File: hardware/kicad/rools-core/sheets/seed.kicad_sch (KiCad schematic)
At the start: 1 part

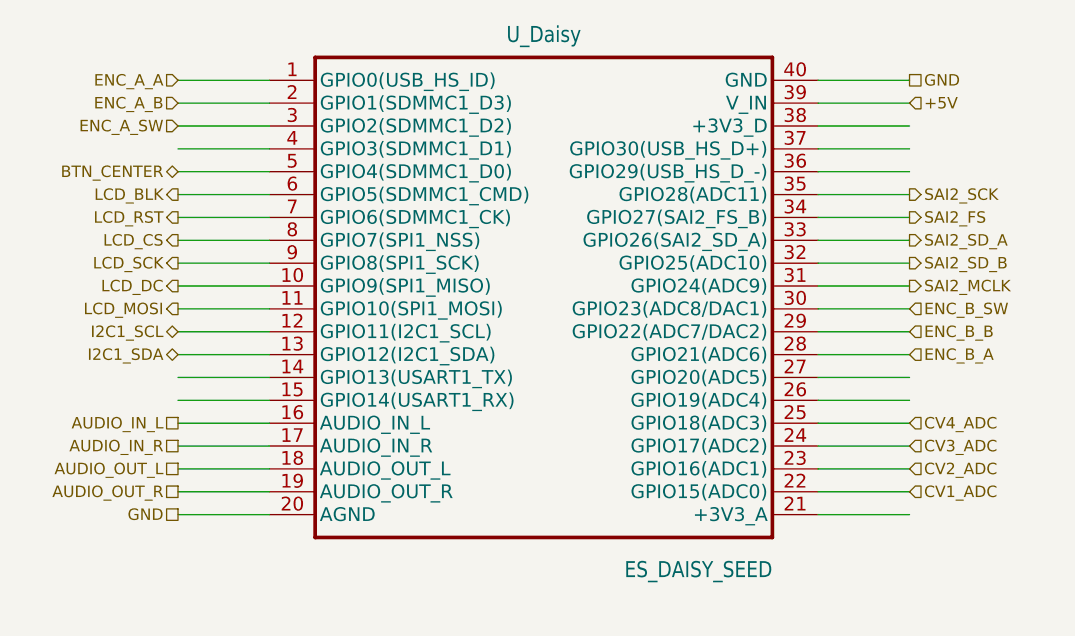
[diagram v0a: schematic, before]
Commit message: Wire rools-core KiCad sheets with global labels and UI peripherals.
Migrate inter-sheet nets to global labels and flesh out UI, power, and
child-sheet power entry so net names align with pins.h for PCB routing.

Co-authored-by: Cursor <cursoragent@cursor.com>
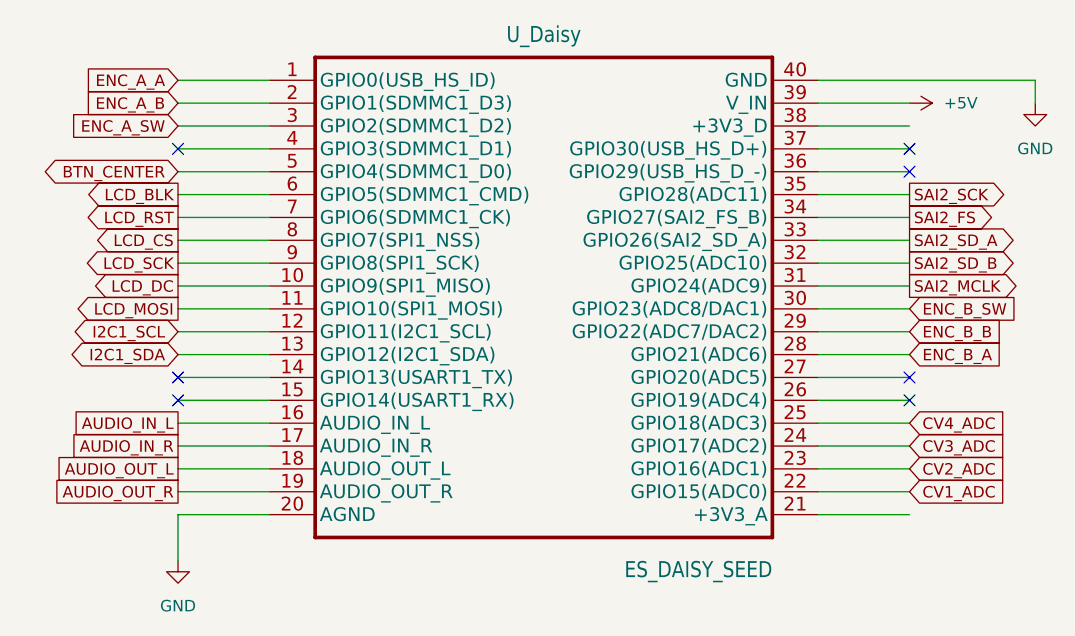
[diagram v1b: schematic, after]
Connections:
- no-connect marks 0 -> 7

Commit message: Add QSPI settings persistence, CV calibration app, and CV output driver.
Co-authored-by: Cursor <cursoragent@cursor.com>
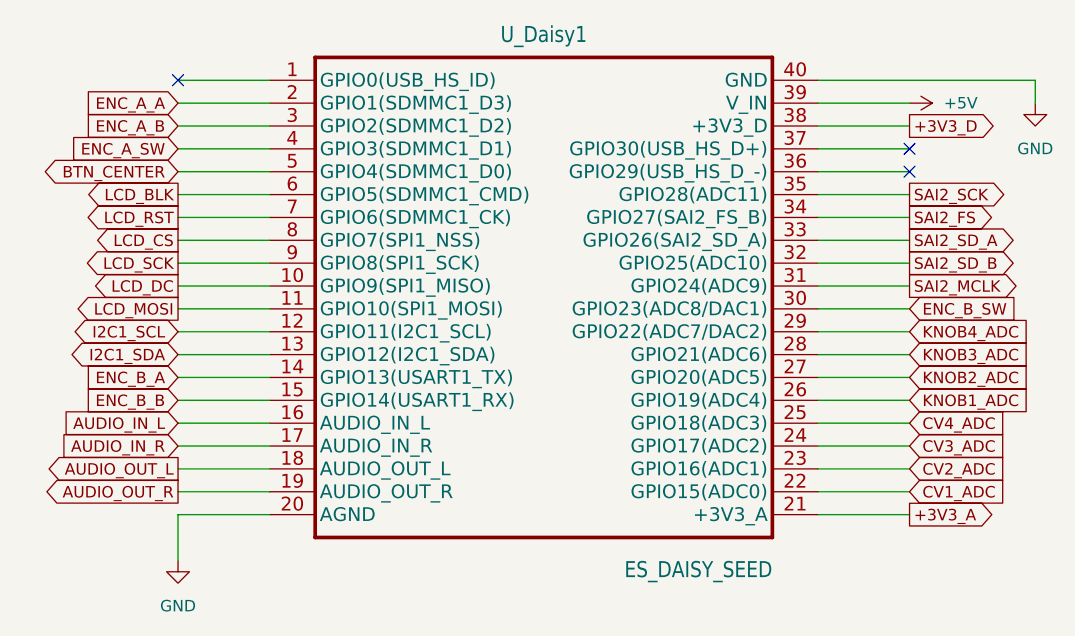
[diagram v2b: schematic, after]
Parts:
- renumbered U_Daisy to U_Daisy1
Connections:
- net ENC_A_A: now also U_Daisy1.2 (GPIO1(SDMMC1_D3)); no longer U_Daisy1.1 (GPIO0(USB_HS_ID))
- net ENC_A_B: now also U_Daisy1.3 (GPIO2(SDMMC1_D2)); no longer U_Daisy1.2 (GPIO1(SDMMC1_D3))
- net ENC_A_SW: now also U_Daisy1.4 (GPIO3(SDMMC1_D1)); no longer U_Daisy1.3 (GPIO2(SDMMC1_D2))
- net ENC_B_A: now also U_Daisy1.14 (GPIO13(USART1_TX)); no longer U_Daisy1.28 (GPIO21(ADC6))
- net ENC_B_B: now also U_Daisy1.15 (GPIO14(USART1_RX)); no longer U_Daisy1.29 (GPIO22(ADC7/DAC2))
- net +3V3_A: now reaches U_Daisy1.21 (+3V3_A)
- net KNOB1_ADC: now reaches U_Daisy1.26 (GPIO19(ADC4))
- net KNOB2_ADC: now reaches U_Daisy1.27 (GPIO20(ADC5))
- net +3V3_D: now reaches U_Daisy1.38 (+3V3_D)
- new net KNOB3_ADC: U_Daisy1.28 (GPIO21(ADC6))
- new net KNOB4_ADC: U_Daisy1.29 (GPIO22(ADC7/DAC2))
- no-connect marks 7 -> 3
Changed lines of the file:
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@@
 	)
 	(no_connect
-		(at 172.72 106.68)
-	)
-	(no_connect
-		(at 91.44 106.68)
-	)
-	(no_connect
-		(at 91.44 81.28)
+		(at 91.44 73.66)
 	)
 	(no_connect
 		(at 172.72 81.28)
-	)
-	(no_connect
-		(at 91.44 109.22)
-	)
-	(no_connect
-		(at 172.72 109.22)
 	)
 	(wire
@@
 	)
 	(global_label "AUDIO_OUT_R"
-		(shape passive)
+		(shape output)
 		(at 91.44 119.38 180)
 		(effects
@@
 		)
 	)
+	(global_label "KNOB3_ADC"
+		(shape input)
+		(at 172.72 104.14 0)
+		(fields_autoplaced yes)
+		(effects
+			(font
+				(size 1.27 1.27)
+			)
+			(justify left)
+		)
+		(property "Intersheetrefs" "${INTERSHEET_REFS}"
+			(at 186.807 104.14 0)
+			(hide yes)
+			(show_name no)
+			(do_not_autoplace no)
+			(effects
+				(font
+					(size 1.27 1.27)
+				)
+				(justify left)
+			)
+		)
+	)
 	(global_label "SAI2_FS"
 		(shape output)
@@
 	(global_label "ENC_A_A"
 		(shape input)
-		(at 91.44 73.66 180)
-		(effects
-			(font
-				(size 1.27 1.27)
-			)
-			(justify right)
-		)
-		(property "Intersheetrefs" "${INTERSHEET_REFS}"
-			(at 91.44 73.66 0)
+		(at 91.44 76.2 180)
+		(effects
+			(font
+				(size 1.27 1.27)
+			)
+			(justify right)
+		)
+		(property "Intersheetrefs" "${INTERSHEET_REFS}"
+			(at 91.44 76.2 0)
 			(hide yes)
 			(show_name no)
@@
 	(global_label "ENC_A_SW"
 		(shape input)
-		(at 91.44 78.74 180)
-		(effects
-			(font
-				(size 1.27 1.27)
-			)
-			(justify right)
-		)
-		(property "Intersheetrefs" "${INTERSHEET_REFS}"
-			(at 91.44 78.74 0)
+		(at 91.44 81.28 180)
+		(effects
+			(font
+				(size 1.27 1.27)
+			)
+			(justify right)
+		)
+		(property "Intersheetrefs" "${INTERSHEET_REFS}"
+			(at 91.44 81.28 0)
 			(hide yes)
 			(show_name no)
@@
 	)
 	(global_label "AUDIO_IN_R"
-		(shape passive)
+		(shape input)
 		(at 91.44 114.3 180)
 		(effects
@@
 					(size 1.27 1.27)
 				)
+			)
+		)
+	)
+	(global_label "KNOB4_ADC"
+		(shape input)
+		(at 172.72 101.6 0)
+		(fields_autoplaced yes)
+		(effects
+			(font
+				(size 1.27 1.27)
+			)
+			(justify left)
+		)
+		(property "Intersheetrefs" "${INTERSHEET_REFS}"
+			(at 186.807 101.6 0)
+			(hide yes)
+			(show_name no)
+			(do_not_autoplace no)
+			(effects
+				(font
+					(size 1.27 1.27)
+				)
+				(justify left)
 			)
 		)
@@
 	(global_label "ENC_B_B"
 		(shape input)
-		(at 172.72 101.6 0)
-		(effects
-			(font
-				(size 1.27 1.27)
-			)
-			(justify left)
-		)
-		(property "Intersheetrefs" "${INTERSHEET_REFS}"
-			(at 172.72 101.6 0)
+		(at 91.44 109.22 180)
+		(effects
+			(font
+				(size 1.27 1.27)
+			)
+			(justify right)
+		)
+		(property "Intersheetrefs" "${INTERSHEET_REFS}"
+			(at 91.44 109.22 0)
 			(hide yes)
 			(show_name no)
@@
 	(global_label "ENC_B_A"
 		(shape input)
-		(at 172.72 104.14 0)
-		(effects
-			(font
-				(size 1.27 1.27)
-			)
-			(justify left)
-		)
-		(property "Intersheetrefs" "${INTERSHEET_REFS}"
-			(at 172.72 104.14 0)
+		(at 91.44 106.68 180)
+		(effects
+			(font
+				(size 1.27 1.27)
+			)
+			(justify right)
+		)
+		(property "Intersheetrefs" "${INTERSHEET_REFS}"
+			(at 91.44 106.68 0)
 			(hide yes)
 			(show_name no)
@@
 		)
 	)
+	(global_label "KNOB2_ADC"
+		(shape input)
+		(at 172.72 106.68 0)
+		(fields_autoplaced yes)
+		(effects
+			(font
+				(size 1.27 1.27)
+			)
+			(justify left)
+		)
+		(property "Intersheetrefs" "${INTERSHEET_REFS}"
+			(at 186.807 106.68 0)
+			(hide yes)
+			(show_name no)
+			(do_not_autoplace no)
+			(effects
+				(font
+					(size 1.27 1.27)
+				)
+				(justify left)
+			)
+		)
+	)
+	(global_label "+3V3_D"
+		(shape output)
+		(at 172.72 78.74 0)
+		(fields_autoplaced yes)
+		(effects
+			(font
+				(size 1.27 1.27)
+			)
+			(justify left)
+		)
+		(property "Intersheetrefs" "${INTERSHEET_REFS}"
+			(at 183.1179 78.74 0)
+			(hide yes)
+			(show_name no)
+			(do_not_autoplace no)
+			(effects
+				(font
+					(size 1.27 1.27)
+				)
+				(justify left)
+			)
+		)
+	)
+	(global_label "KNOB1_ADC"
+		(shape input)
+		(at 172.72 109.22 0)
+		(fields_autoplaced yes)
+		(effects
+			(font
+				(size 1.27 1.27)
+			)
+			(justify left)
+		)
+		(property "Intersheetrefs" "${INTERSHEET_REFS}"
+			(at 186.807 109.22 0)
+			(hide yes)
+			(show_name no)
+			(do_not_autoplace no)
+			(effects
+				(font
+					(size 1.27 1.27)
+				)
+				(justify left)
+			)
+		)
+	)
 	(global_label "AUDIO_OUT_L"
-		(shape passive)
+		(shape output)
 		(at 91.44 116.84 180)
 		(effects
@@
 	(global_label "ENC_A_B"
 		(shape input)
-		(at 91.44 76.2 180)
-		(effects
-			(font
-				(size 1.27 1.27)
-			)
-			(justify right)
-		)
-		(property "Intersheetrefs" "${INTERSHEET_REFS}"
-			(at 91.44 76.2 0)
+		(at 91.44 78.74 180)
+		(effects
+			(font
+				(size 1.27 1.27)
+			)
+			(justify right)
+		)
+		(property "Intersheetrefs" "${INTERSHEET_REFS}"
+			(at 91.44 78.74 0)
 			(hide yes)
 			(show_name no)
@@
 	)
 	(global_label "AUDIO_IN_L"
-		(shape passive)
+		(shape input)
 		(at 91.44 111.76 180)
 		(effects
@@
 					(size 1.27 1.27)
 				)
+			)
+		)
+	)
+	(global_label "+3V3_A"
+		(shape output)
+		(at 172.72 121.92 0)
+		(fields_autoplaced yes)
+		(effects
+			(font
+				(size 1.27 1.27)
+			)
+			(justify left)
+		)
+		(property "Intersheetrefs" "${INTERSHEET_REFS}"
+			(at 182.9365 121.92 0)
+			(hide yes)
+			(show_name no)
+			(do_not_autoplace no)
+			(effects
+				(font
+					(size 1.27 1.27)
+				)
+				(justify left)
 			)
 		)
@@
 		(in_pos_files yes)
 		(dnp no)
-		(property "Reference" "U_Daisy"
+		(property "Reference" "U_Daisy1"
 			(at 132.08 68.58 0)
 			(show_name no)
@@
 			(project "rools-core"
 				(path "/e63e39d7-6ac0-4ffd-8aa3-1841a4541b55/5303161d-9629-4121-9b8d-eb317bf3612e"
-					(reference "U_Daisy")
+					(reference "U_Daisy1")
 					(unit 1)
 				)
@@
 		(dnp no)
 		(fields_autoplaced yes)
-		(property "Reference" "#PWR010"
+		(property "Reference" "#PWR03"
 			(at 186.69 82.55 0)
 			(hide yes)
@@
 			(project "rools-core"
 				(path "/e63e39d7-6ac0-4ffd-8aa3-1841a4541b55/5303161d-9629-4121-9b8d-eb317bf3612e"
-					(reference "#PWR010")
+					(reference "#PWR03")
 					(unit 1)
 				)
@@
 		(dnp no)
 		(fields_autoplaced yes)
-		(property "Reference" "#PWR012"
+		(property "Reference" "#PWR01"
 			(at 91.44 133.35 0)
 			(hide yes)
@@
 			(project "rools-core"
 				(path "/e63e39d7-6ac0-4ffd-8aa3-1841a4541b55/5303161d-9629-4121-9b8d-eb317bf3612e"
-					(reference "#PWR012")
+					(reference "#PWR01")
 					(unit 1)
 				)
@@
 		(dnp no)
 		(fields_autoplaced yes)
-		(property "Reference" "#PWR011"
+		(property "Reference" "#PWR02"
 			(at 168.91 76.2 0)
 			(hide yes)
@@
 			(project "rools-core"
 				(path "/e63e39d7-6ac0-4ffd-8aa3-1841a4541b55/5303161d-9629-4121-9b8d-eb317bf3612e"
-					(reference "#PWR011")
+					(reference "#PWR02")
 					(unit 1)
 				)

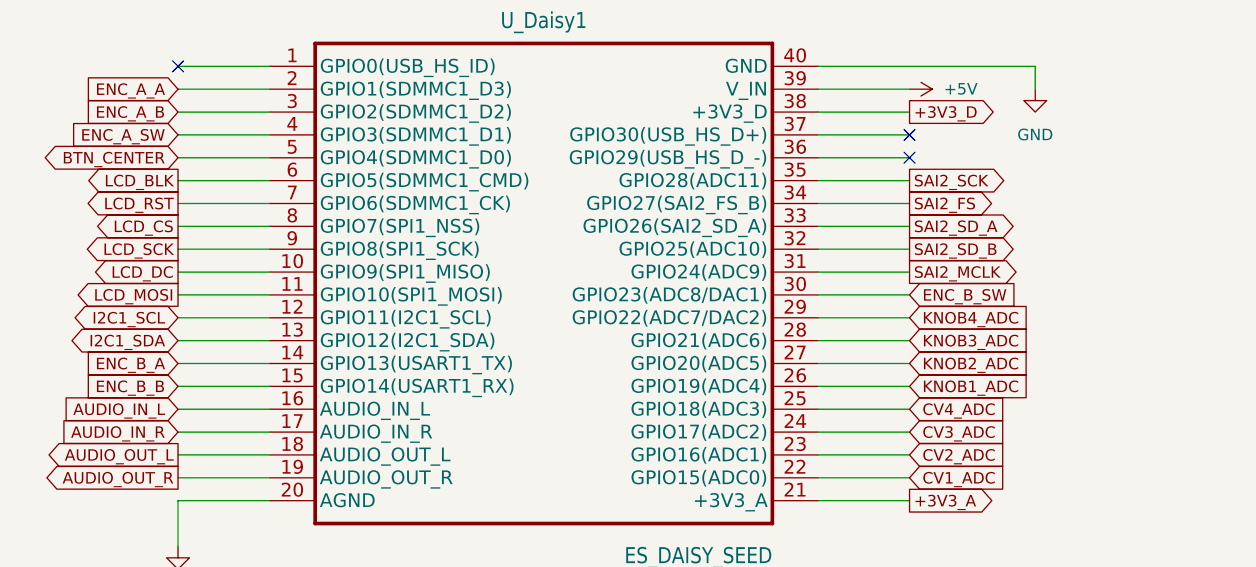
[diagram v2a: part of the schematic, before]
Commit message: Align Core with onboard audio and split CV/Knob ADC architecture.
Document Seed pin16–19 + TL074 (no PCM3060), 8-way ADC firmware synthesis, Enc/Knob pin remap, EXTI_PWR on D28, and update KiCad seed/CV/audio sheets accordingly.

Co-authored-by: Cursor <cursoragent@cursor.com>
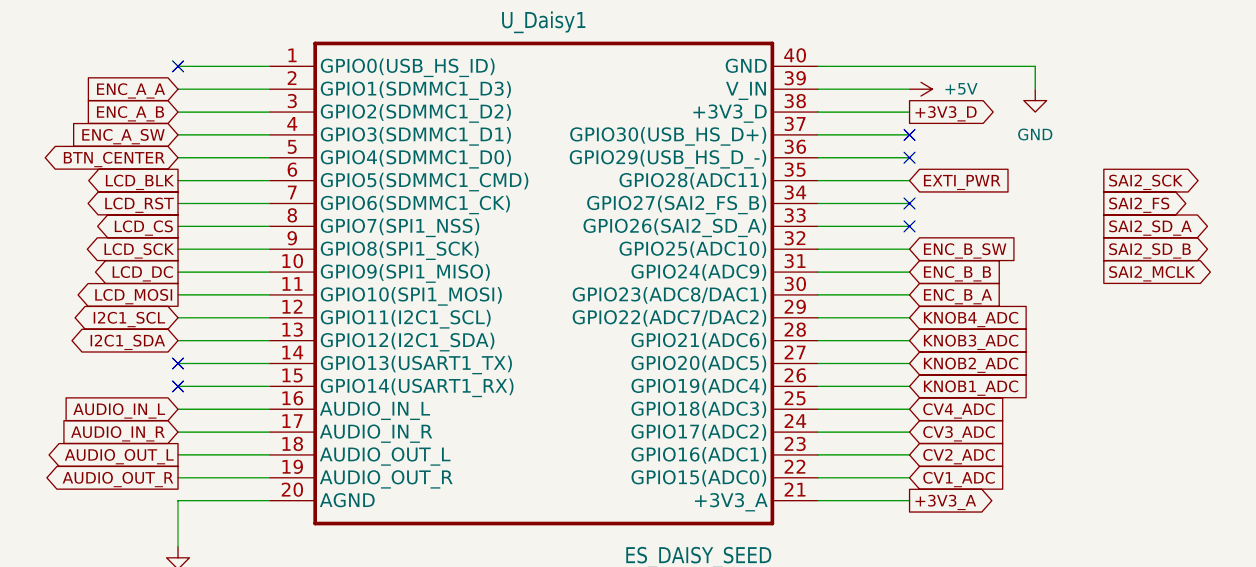
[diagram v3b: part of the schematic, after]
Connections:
- net ENC_B_A: now also U_Daisy1.30 (GPIO23(ADC8/DAC1)); no longer U_Daisy1.14 (GPIO13(USART1_TX))
- net ENC_B_B: now also U_Daisy1.31 (GPIO24(ADC9)); no longer U_Daisy1.15 (GPIO14(USART1_RX))
- net ENC_B_SW: now also U_Daisy1.32 (GPIO25(ADC10)); no longer U_Daisy1.30 (GPIO23(ADC8/DAC1))
- net SAI2_FS: no longer U_Daisy1.34 (GPIO27(SAI2_FS_B))
- net SAI2_MCLK: no longer U_Daisy1.31 (GPIO24(ADC9))
- net SAI2_SCK: no longer U_Daisy1.35 (GPIO28(ADC11))
- net SAI2_SD_A: no longer U_Daisy1.33 (GPIO26(SAI2_SD_A))
- net SAI2_SD_B: no longer U_Daisy1.32 (GPIO25(ADC10))
- new net EXTI_PWR: U_Daisy1.35 (GPIO28(ADC11))
- no-connect marks 3 -> 7
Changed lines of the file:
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@@
+	)
+	(no_connect
+		(at 172.72 91.44)
 	)
 	(no_connect
@@
 	)
 	(no_connect
+		(at 91.44 106.68)
+	)
+	(no_connect
 		(at 172.72 81.28)
 	)
+	(no_connect
+		(at 91.44 109.22)
+	)
+	(no_connect
+		(at 172.72 88.9)
+	)
 	(wire
 		(pts
@@
 	(global_label "SAI2_SCK"
 		(shape output)
+		(at 194.31 86.36 0)
+		(effects
+			(font
+				(size 1.27 1.27)
+			)
+			(justify left)
+		)
+		(property "Intersheetrefs" "${INTERSHEET_REFS}"
+			(at 194.31 86.36 0)
+			(hide yes)
+			(show_name no)
+			(do_not_autoplace no)
+			(effects
+				(font
+					(size 1.27 1.27)
+				)
+			)
+		)
+	)
+	(global_label "EXTI_PWR"
+		(shape input)
 		(at 172.72 86.36 0)
-		(effects
-			(font
-				(size 1.27 1.27)
-			)
-			(justify left)
-		)
-		(property "Intersheetrefs" "${INTERSHEET_REFS}"
-			(at 172.72 86.36 0)
-			(hide yes)
-			(show_name no)
-			(do_not_autoplace no)
-			(effects
-				(font
-					(size 1.27 1.27)
-				)
+		(fields_autoplaced yes)
+		(effects
+			(font
+				(size 1.27 1.27)
+			)
+			(justify left)
+		)
+		(property "Intersheetrefs" "${INTERSHEET_REFS}"
+			(at 184.6902 86.36 0)
+			(hide yes)
+			(show_name no)
+			(do_not_autoplace no)
+			(effects
+				(font
+					(size 1.27 1.27)
+				)
+				(justify left)
 			)
 		)
@@
 	(global_label "ENC_B_SW"
 		(shape input)
-		(at 172.72 99.06 0)
-		(effects
-			(font
-				(size 1.27 1.27)
-			)
-			(justify left)
-		)
-		(property "Intersheetrefs" "${INTERSHEET_REFS}"
-			(at 172.72 99.06 0)
+		(at 172.72 93.98 0)
+		(effects
+			(font
+				(size 1.27 1.27)
+			)
+			(justify left)
+		)
+		(property "Intersheetrefs" "${INTERSHEET_REFS}"
+			(at 172.72 93.98 0)
 			(hide yes)
 			(show_name no)
@@
 	(global_label "SAI2_FS"
 		(shape output)
-		(at 172.72 88.9 0)
-		(effects
-			(font
-				(size 1.27 1.27)
-			)
-			(justify left)
-		)
-		(property "Intersheetrefs" "${INTERSHEET_REFS}"
-			(at 172.72 88.9 0)
+		(at 194.31 88.9 0)
+		(effects
+			(font
+				(size 1.27 1.27)
+			)
+			(justify left)
+		)
+		(property "Intersheetrefs" "${INTERSHEET_REFS}"
+			(at 194.31 88.9 0)
 			(hide yes)
 			(show_name no)
@@
 	(global_label "ENC_B_B"
 		(shape input)
-		(at 91.44 109.22 180)
-		(effects
-			(font
-				(size 1.27 1.27)
-			)
-			(justify right)
-		)
-		(property "Intersheetrefs" "${INTERSHEET_REFS}"
-			(at 91.44 109.22 0)
+		(at 172.72 96.52 0)
+		(effects
+			(font
+				(size 1.27 1.27)
+			)
+			(justify left)
+		)
+		(property "Intersheetrefs" "${INTERSHEET_REFS}"
+			(at 172.72 96.52 0)
 			(hide yes)
 			(show_name no)
@@
 	(global_label "SAI2_SD_A"
 		(shape output)
-		(at 172.72 91.44 0)
-		(effects
-			(font
-				(size 1.27 1.27)
-			)
-			(justify left)
-		)
-		(property "Intersheetrefs" "${INTERSHEET_REFS}"
-			(at 172.72 91.44 0)
+		(at 194.31 91.44 0)
+		(effects
+			(font
+				(size 1.27 1.27)
+			)
+			(justify left)
+		)
+		(property "Intersheetrefs" "${INTERSHEET_REFS}"
+			(at 194.31 91.44 0)
 			(hide yes)
 			(show_name no)
@@
 	(global_label "ENC_B_A"
 		(shape input)
-		(at 91.44 106.68 180)
-		(effects
-			(font
-				(size 1.27 1.27)
-			)
-			(justify right)
-		)
-		(property "Intersheetrefs" "${INTERSHEET_REFS}"
-			(at 91.44 106.68 0)
+		(at 172.72 99.06 0)
+		(effects
+			(font
+				(size 1.27 1.27)
+			)
+			(justify left)
+		)
+		(property "Intersheetrefs" "${INTERSHEET_REFS}"
+			(at 172.72 99.06 0)
 			(hide yes)
 			(show_name no)
@@
 	(global_label "SAI2_MCLK"
 		(shape output)
-		(at 172.72 96.52 0)
-		(effects
-			(font
-				(size 1.27 1.27)
-			)
-			(justify left)
-		)
-		(property "Intersheetrefs" "${INTERSHEET_REFS}"
-			(at 172.72 96.52 0)
+		(at 194.31 96.52 0)
+		(effects
+			(font
+				(size 1.27 1.27)
+			)
+			(justify left)
+		)
+		(property "Intersheetrefs" "${INTERSHEET_REFS}"
+			(at 194.31 96.52 0)
 			(hide yes)
 			(show_name no)
@@
 	(global_label "SAI2_SD_B"
 		(shape output)
-		(at 172.72 93.98 0)
-		(effects
-			(font
-				(size 1.27 1.27)
-			)
-			(justify left)
-		)
-		(property "Intersheetrefs" "${INTERSHEET_REFS}"
-			(at 172.72 93.98 0)
-			(hide yes)
-			(show_name no)
+		(at 194.31 93.98 0)
+		(effects
+			(font
+				(size 1.27 1.27)
+			)
+			(justify left)
+		)
+		(property "Intersheetrefs" "${INTERSHEET_REFS}"
+			(at 194.31 93.98 0)
+			(hide yes)
+			(show_name no)
